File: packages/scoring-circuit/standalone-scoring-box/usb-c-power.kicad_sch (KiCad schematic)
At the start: 28 parts, among them J12 PD service: GND SDA SCL, Q4 DMN2056U-7, Q5 DMN2056U-7, U20 TPS259470LRPWR, U22 TPS70933DBVR, U5 STUSB4500QTR, U6 REC30K-2405SZ

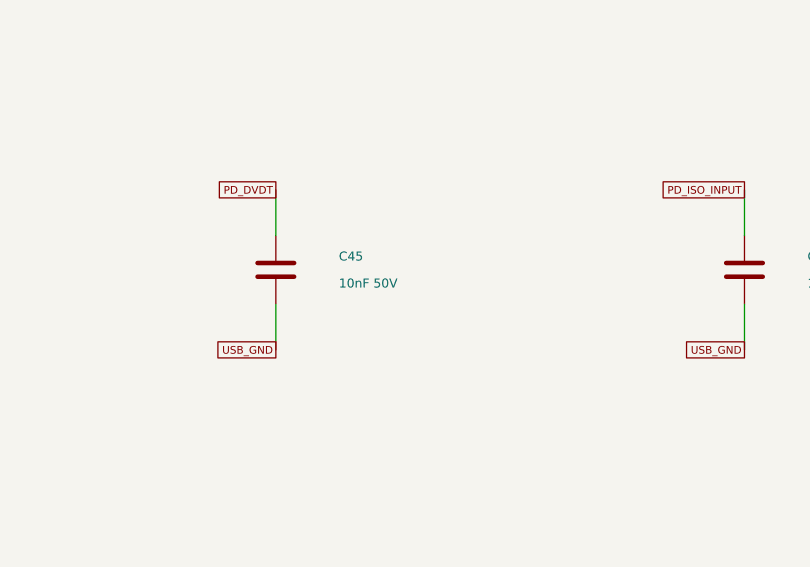
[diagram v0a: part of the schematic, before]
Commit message: feat(scoring-circuit): prepare standalone power and assembly handoff
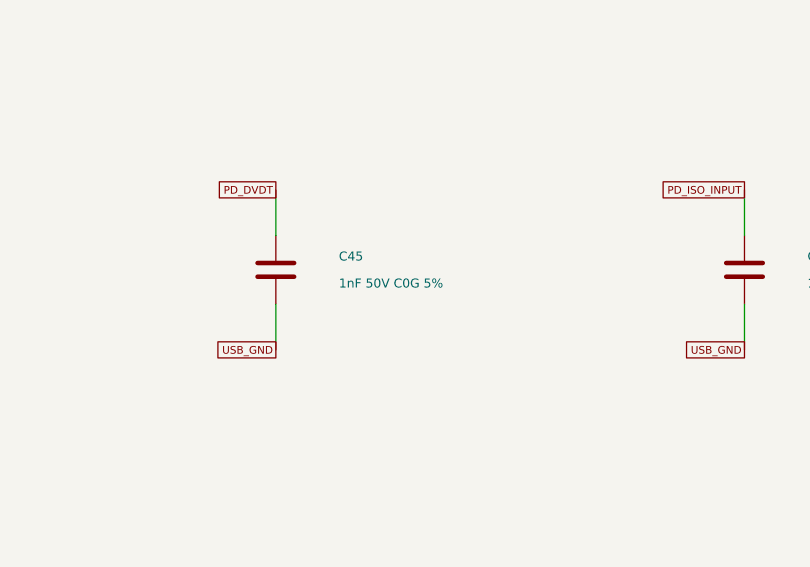
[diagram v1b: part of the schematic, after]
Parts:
- C45: value 10nF 50V -> 1nF 50V C0G 5%; MPN C1608X7R1H103K080AA -> C1608C0G1H102J080AA
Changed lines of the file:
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@@
 (symbol (lib_id "Device:R") (at 204.47 154.94 0) (unit 1) (in_bom yes) (on_board yes) (dnp no) (property "Reference" "R97" (at 211.47 153.44 0) (effects (font (size 1 1)) (justify left))) (property "Value" "10k 0.1%" (at 211.47 156.44 0) (effects (font (size 1 1)) (justify left))) (property "Footprint" "Resistor_SMD:R_0603_1608Metric" (at 314.96 265.43 0) (effects (font (size 1 1)) (hide yes))) (property "Manufacturer" "YAGEO" (at 314.96 265.43 0) (effects (font (size 1 1)) (hide yes))) (property "MPN" "RT0603BRD0710KL" (at 314.96 265.43 0) (effects (font (size 1 1)) (hide yes))) (property "Datasheet" "https://www.yageogroup.com/component-documentation/download/specsheet/RT0603BRD0710KL" (at 314.96 265.43 0) (effects (font (size 1 1)) (hide yes))) (pin "1") (pin "2") (instances (project "standalone-scoring-box" (path "/95251ad8-e338-4d8f-a50b-ff3c23d840b3/08af3609-5a9b-46bf-abfd-61b07bd88d20" (reference "R97") (unit 1)))))
 (symbol (lib_id "Device:R") (at 255.27 154.94 0) (unit 1) (in_bom yes) (on_board yes) (dnp no) (property "Reference" "R98" (at 262.27 153.44 0) (effects (font (size 1 1)) (justify left))) (property "Value" "1.37k 1%" (at 262.27 156.44 0) (effects (font (size 1 1)) (justify left))) (property "Footprint" "Resistor_SMD:R_0603_1608Metric" (at 439.42 265.43 0) (effects (font (size 1 1)) (hide yes))) (property "Manufacturer" "YAGEO" (at 439.42 265.43 0) (effects (font (size 1 1)) (hide yes))) (property "MPN" "RC0603FR-071K37L" (at 439.42 265.43 0) (effects (font (size 1 1)) (hide yes))) (property "Datasheet" "https://www.yageogroup.com/component-documentation/download/specsheet/RC0603FR-071K37L" (at 439.42 265.43 0) (effects (font (size 1 1)) (hide yes))) (pin "1") (pin "2") (instances (project "standalone-scoring-box" (path "/95251ad8-e338-4d8f-a50b-ff3c23d840b3/08af3609-5a9b-46bf-abfd-61b07bd88d20" (reference "R98") (unit 1)))))
-(symbol (lib_id "Device:C") (at 307.34 154.94 0) (unit 1) (in_bom yes) (on_board yes) (dnp no) (property "Reference" "C45" (at 314.34 153.44 0) (effects (font (size 1 1)) (justify left))) (property "Value" "10nF 50V" (at 314.34 156.44 0) (effects (font (size 1 1)) (justify left))) (property "Footprint" "Capacitor_SMD:C_0603_1608Metric" (at 565.15 265.43 0) (effects (font (size 1 1)) (hide yes))) (property "Manufacturer" "TDK" (at 565.15 265.43 0) (effects (font (size 1 1)) (hide yes))) (property "MPN" "C1608X7R1H103K080AA" (at 565.15 265.43 0) (effects (font (size 1 1)) (hide yes))) (property "Datasheet" "https://product.tdk.com/en/search/capacitor/ceramic/mlcc/info?part_no=C1608X7R1H103K080AA" (at 565.15 265.43 0) (effects (font (size 1 1)) (hide yes))) (pin "1") (pin "2") (instances (project "standalone-scoring-box" (path "/95251ad8-e338-4d8f-a50b-ff3c23d840b3/08af3609-5a9b-46bf-abfd-61b07bd88d20" (reference "C45") (unit 1)))))
+(symbol (lib_id "Device:C") (at 307.34 154.94 0) (unit 1) (in_bom yes) (on_board yes) (dnp no) (property "Reference" "C45" (at 314.34 153.44 0) (effects (font (size 1 1)) (justify left))) (property "Value" "1nF 50V C0G 5%" (at 314.34 156.44 0) (effects (font (size 1 1)) (justify left))) (property "Footprint" "Capacitor_SMD:C_0603_1608Metric" (at 565.15 265.43 0) (effects (font (size 1 1)) (hide yes))) (property "Manufacturer" "TDK" (at 565.15 265.43 0) (effects (font (size 1 1)) (hide yes))) (property "MPN" "C1608C0G1H102J080AA" (at 565.15 265.43 0) (effects (font (size 1 1)) (hide yes))) (property "Datasheet" "https://product.tdk.com/en/search/capacitor/ceramic/mlcc/info?part_no=C1608C0G1H102J080AA" (at 565.15 265.43 0) (effects (font (size 1 1)) (hide yes))) (pin "1") (pin "2") (instances (project "standalone-scoring-box" (path "/95251ad8-e338-4d8f-a50b-ff3c23d840b3/08af3609-5a9b-46bf-abfd-61b07bd88d20" (reference "C45") (unit 1)))))
 (symbol (lib_id "Device:C") (at 359.41 154.94 0) (unit 1) (in_bom yes) (on_board yes) (dnp no) (property "Reference" "C46" (at 366.41 153.44 0) (effects (font (size 1 1)) (justify left))) (property "Value" "100nF 50V" (at 366.41 156.44 0) (effects (font (size 1 1)) (justify left))) (property "Footprint" "Capacitor_SMD:C_0805_2012Metric" (at 689.61 265.43 0) (effects (font (size 1 1)) (hide yes))) (property "Manufacturer" "TDK" (at 689.61 265.43 0) (effects (font (size 1 1)) (hide yes))) (property "MPN" "C2012X7R2A104K125AA" (at 689.61 265.43 0) (effects (font (size 1 1)) (hide yes))) (property "Datasheet" "https://product.tdk.com/en/search/capacitor/ceramic/mlcc/info?part_no=C2012X7R2A104K125AA" (at 689.61 265.43 0) (effects (font (size 1 1)) (hide yes))) (pin "1") (pin "2") (instances (project "standalone-scoring-box" (path "/95251ad8-e338-4d8f-a50b-ff3c23d840b3/08af3609-5a9b-46bf-abfd-61b07bd88d20" (reference "C46") (unit 1)))))
 (symbol (lib_id "Device:C") (at 48.26 204.47 0) (unit 1) (in_bom yes) (on_board yes) (dnp no) (property "Reference" "C47" (at 55.26 202.97 0) (effects (font (size 1 1)) (justify left))) (property "Value" "10uF 50V" (at 55.26 205.97 0) (effects (font (size 1 1)) (justify left))) (property "Footprint" "Capacitor_SMD:C_1210_3225Metric" (at 64.77 355.6 0) (effects (font (size 1 1)) (hide yes))) (property "Datasheet" "https://product.tdk.com/en/search/capacitor/ceramic/mlcc/info?part_no=C3225X7R1H106K250AC" (at 64.77 355.6 0) (effects (font (size 1 1)) (hide yes))) (property "Manufacturer" "TDK" (at 64.77 355.6 0) (effects (font (size 1 1)) (hide yes))) (property "MPN" "C3225X7R1H106K250AC" (at 64.77 355.6 0) (effects (font (size 1 1)) (hide yes))) (pin "1") (pin "2") (instances (project "standalone-scoring-box" (path "/95251ad8-e338-4d8f-a50b-ff3c23d840b3/08af3609-5a9b-46bf-abfd-61b07bd88d20" (reference "C47") (unit 1)))))

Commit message: fix(scoring-circuit): resolve standalone assembly sourcing matches
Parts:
- C36, C73: LCSC (none) -> C91185; MPN C2012X7R1H105K125AB -> CC0805KKX7R9BB105; Manufacturer TDK -> YAGEO
- C37, C38: LCSC (none) -> C559769; MPN C1608X7R1H105K080AB -> CC0603KRX7R9BB105; Manufacturer TDK -> YAGEO
- C45: LCSC (none) -> C106246; MPN C1608C0G1H102J080AA -> CC0603JRNPO9BN102; Manufacturer TDK -> YAGEO
- C46: LCSC (none) -> C106243; MPN C2012X7R2A104K125AA -> CC0805KKX7R0BB104; Manufacturer TDK -> YAGEO
- C47: LCSC (none) -> C432929; MPN C3225X7R1H106K250AC -> C3225X7R1H106KT000E
- C49: LCSC (none) -> C342827; MPN C3216X7R1C106K160AC -> C3216X7R1C106KT000N
- R98: LCSC (none) -> C4209564; MPN RC0603FR-071K37L -> CRCW06031K37FKEA; Manufacturer YAGEO -> Vishay
